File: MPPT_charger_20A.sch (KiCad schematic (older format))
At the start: 6 parts, among them J5 CONN_01X03

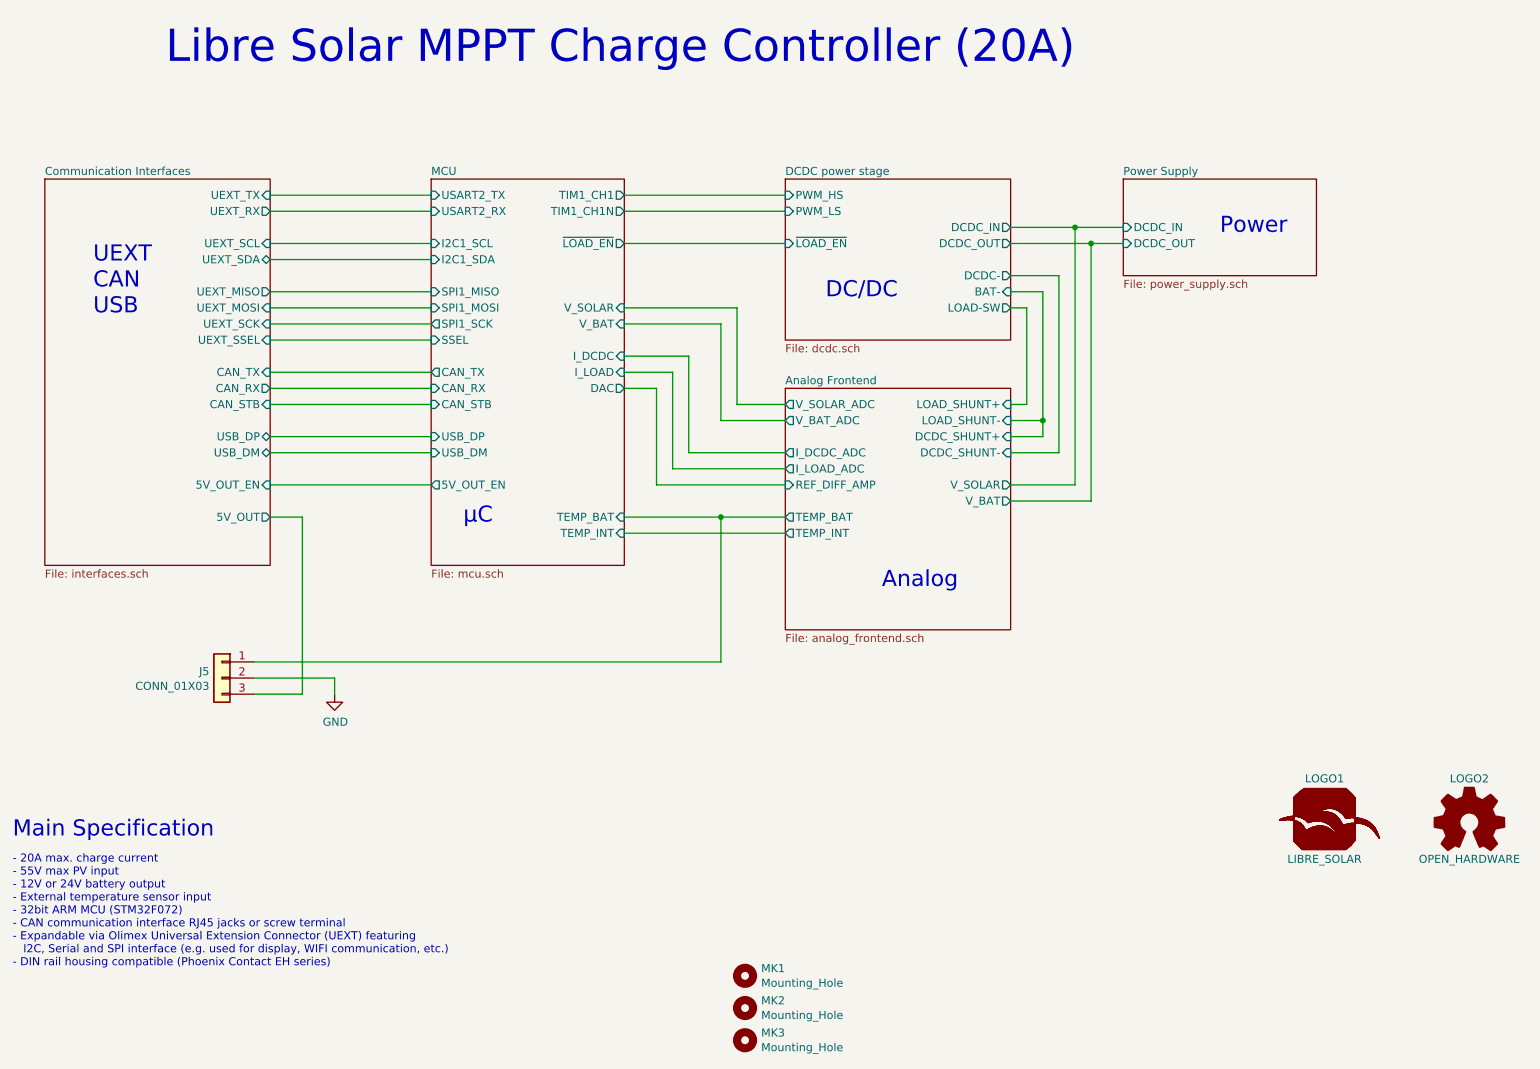
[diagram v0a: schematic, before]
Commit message: Bus power supply from battery instead of 10V rail
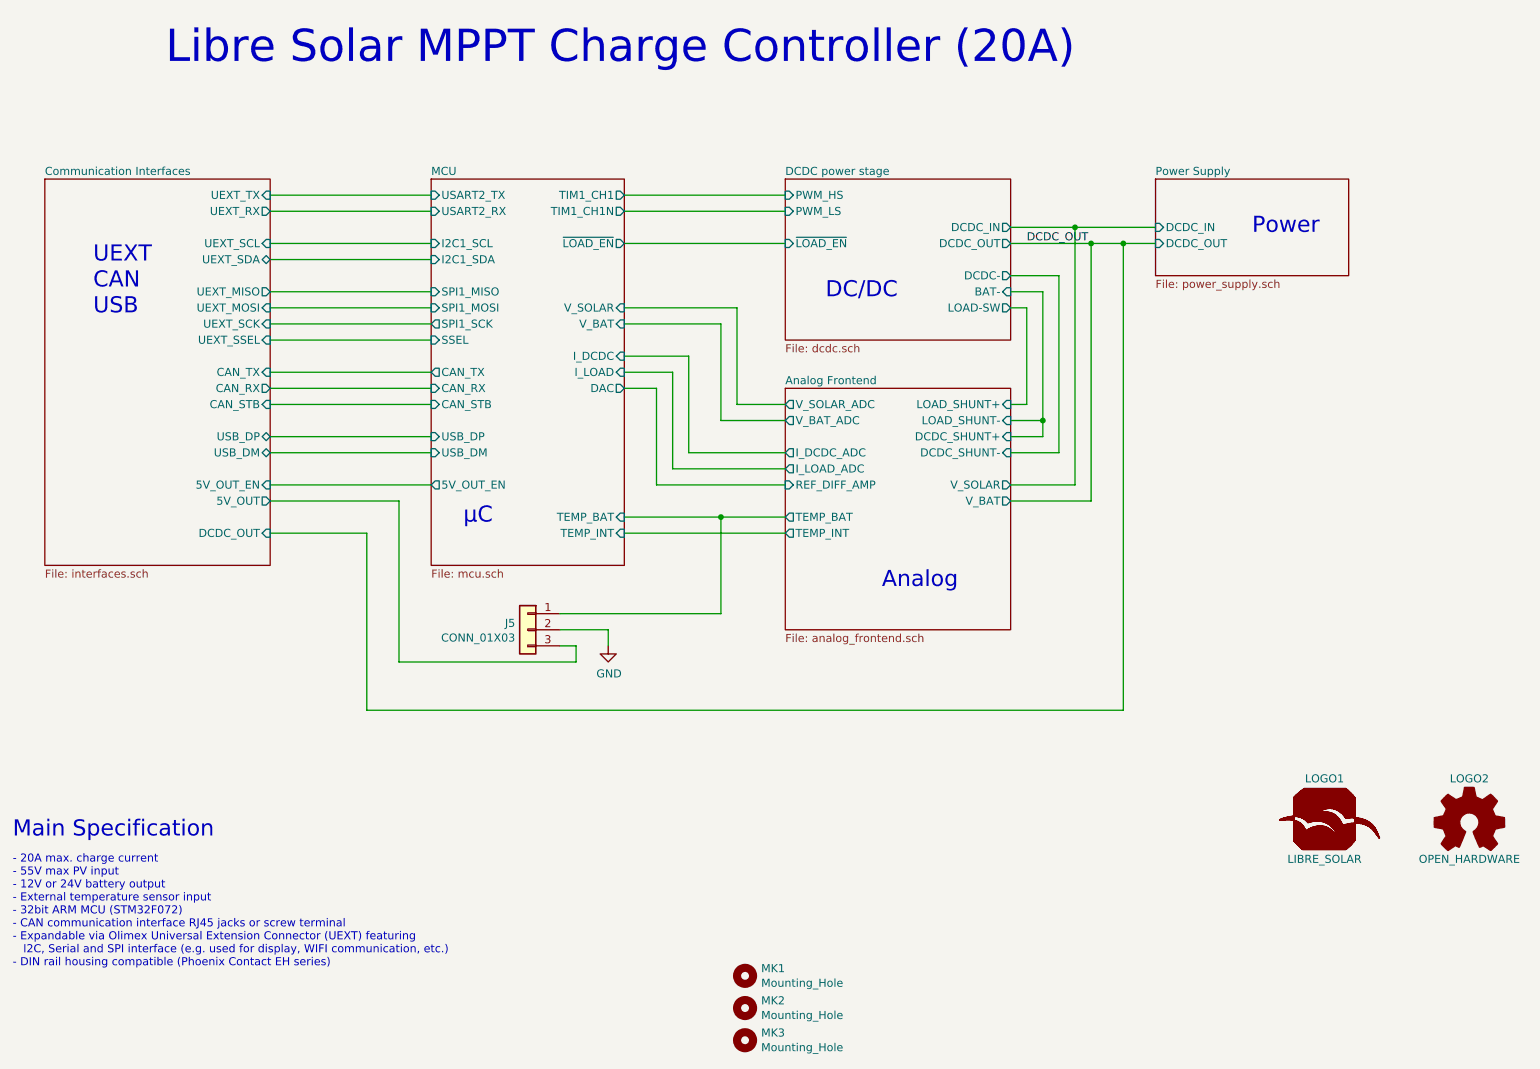
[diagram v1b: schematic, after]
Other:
- moved on the sheet: J5
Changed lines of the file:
@@
 $EndSheet
 $Sheet
-S 8400 2100 1200 600
+S 8600 2100 1200 600
 U 58C18D5C
 F0 "Power Supply" 50
 F1 "power_supply.sch" 50
-F2 "DCDC_OUT" I L 8400 2500 50
-F3 "DCDC_IN" I L 8400 2400 50
+F2 "DCDC_OUT" I L 8600 2500 50
+F3 "DCDC_IN" I L 8600 2400 50
 $EndSheet
 Wire Wire Line
@@
 F13 "CAN_TX" I R 3100 3300 50
 F14 "CAN_STB" I R 3100 3500 50
-F15 "5V_OUT" O R 3100 4200 50
+F15 "5V_OUT" O R 3100 4100 50
 F16 "5V_OUT_EN" I R 3100 4000 50
+F17 "DCDC_OUT" I R 3100 4300 50
 $EndSheet
 Wire Wire Line
@@
 $EndComp
 Wire Wire Line
-	7700 2400 8400 2400
-Wire Wire Line
-	7700 2500 8400 2500
+	7700 2400 8600 2400
+Wire Wire Line
+	7700 2500 8600 2500
 $Sheet
 S 6300 3400 1400 1500
@@
 Text Notes 6900 4650 0    100  ~ 0
 Analog
-Text Notes 9000 2450 0    100  ~ 0
+Text Notes 9200 2450 0    100  ~ 0
 Power
 Wire Wire Line
@@
 	5500 4000 6300 4000
 Wire Wire Line
-	6300 4200 5300 4200
+	5300 4200 6300 4200
 Wire Wire Line
 	5300 4300 6300 4300
@@
 L Connector:Conn_01x03 J5
 U 1 1 59553D8B
-P 2800 5200
-F 0 "J5" H 2878 5241 50  0000 L CNN
-F 1 "CONN_01X03" H 2878 5150 50  0000 L CNN
-F 2 "LibreSolar:Phoenix_Contact_MC_1,5_3-G-3,81" H 2800 5200 50  0001 C CNN
-F 3 "" H 2800 5200 50  0001 C CNN
-F 4 "Phoenix Contact" H 0   0   60  0001 C CNN "Manufacturer"
-F 5 "1803280" H 0   0   60  0001 C CNN "PartNumber"
-	1    2800 5200
+P 4700 4900
+F 0 "J5" H 4778 4941 50  0000 L CNN
+F 1 "CONN_01X03" H 4778 4850 50  0000 L CNN
+F 2 "LibreSolar:Phoenix_Contact_MC_1,5_3-G-3,81" H 4700 4900 50  0001 C CNN
+F 3 "" H 4700 4900 50  0001 C CNN
+F 4 "Phoenix Contact" H 1900 -300 60  0001 C CNN "Manufacturer"
+F 5 "1803280" H 1900 -300 60  0001 C CNN "PartNumber"
+	1    4700 4900
 	-1   0    0    -1
 $EndComp
@@
 L power:GND #PWR01
 U 1 1 59553D94
-P 3500 5300
-F 0 "#PWR01" H 3500 5050 50  0001 C CNN
-F 1 "GND" H 3505 5127 50  0000 C CNN
-F 2 "" H 3500 5300 50  0001 C CNN
-F 3 "" H 3500 5300 50  0001 C CNN
-	1    3500 5300
-	1    0    0    -1
-$EndComp
-Wire Wire Line
-	3000 5100 5900 5100
-Wire Wire Line
-	5900 5100 5900 4200
+P 5200 5000
+F 0 "#PWR01" H 5200 4750 50  0001 C CNN
+F 1 "GND" H 5205 4827 50  0000 C CNN
+F 2 "" H 5200 5000 50  0001 C CNN
+F 3 "" H 5200 5000 50  0001 C CNN
+	1    5200 5000
+	1    0    0    -1
+$EndComp
+Wire Wire Line
+	4900 4800 5900 4800
+Wire Wire Line
+	5900 4800 5900 4200
 Connection ~ 5900 4200
 Wire Wire Line
-	3000 5200 3500 5200
-Wire Wire Line
-	3500 5200 3500 5300
-Wire Wire Line
-	3100 4200 3300 4200
-Wire Wire Line
-	3300 4200 3300 5300
-Wire Wire Line
-	3300 5300 3000 5300
+	4900 4900 5200 4900
+Wire Wire Line
+	5200 4900 5200 5000
+Wire Wire Line
+	5000 5000 4900 5000
 Wire Wire Line
 	3100 4000 4100 4000
+Wire Wire Line
+	5000 5000 5000 5100
+Wire Wire Line
+	5000 5100 3900 5100
+Wire Wire Line
+	3900 5100 3900 4100
+Wire Wire Line
+	3900 4100 3100 4100
+Wire Wire Line
+	3100 4300 3700 4300
+Wire Wire Line
+	3700 4300 3700 5400
+Wire Wire Line
+	3700 5400 8400 5400
+Wire Wire Line
+	8400 5400 8400 2500
+Connection ~ 8400 2500
+Text Label 7800 2500 0    50   ~ 0
+DCDC_OUT
 $EndSCHEMATC

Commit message: Revision 0.9 for first small production batch - Switchable power supply for bus and UEXT (to be make sure to reach very low power consumption during LVD conditions) - MLCCs for EMC added to each high power input/output - Re-arrangement of some connectors after initial tests with housing
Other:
- note added: "- 12V or 24V battery voltage\n- 20A max. charge current\n- 55V max. solar input\n- External temperature sensor input\n- 32bit ARM MCU (STM32F072)\n- CAN communication interface RJ45 jacks incl. bus power supply\n- Expandable via Olimex Universal Extension Connector (UEXT) featuring\n I2C, Serial and SPI interface (e.g. used for display, WIFI communication, etc.)\n- Prepared for Hammond Mfg. 1591X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"
- note added: "MCU"
- note added: "UEXT\n\nCAN\n\nUSB"
- note removed: "- 20A max. charge current\n- 55V max PV input\n- 12V or 24V battery output\n- External temperature sensor input\n- 32bit ARM MCU (STM32F072)\n- CAN communication interface RJ45 jacks or screw terminal\n- Expandable via Olimex Universal Extension Connector (UEXT) featuring\n I2C, Serial and SPI interface (e.g. used for display, WIFI communication, etc.)\n- DIN rail housing compatible (Phoenix Cont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"
- note removed: "UEXT\nCAN\nUSB"
- note removed: "µC"
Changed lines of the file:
@@
 Sheet 1 6
 Title "MPPT Charger 20A"
-Date "2017-03-06"
-Rev "0.7"
+Date "2017-12-11"
+Rev "0.9"
 Comp "Libre Solar"
 Comment1 "Author: Martin Jäger"
@@
 F2 "PWM_HS" I L 6300 2200 50
 F3 "PWM_LS" I L 6300 2300 50
-F4 "~LOAD_EN" I L 6300 2500 50
-F5 "BAT-" I R 7700 2800 50
-F6 "DCDC_OUT" O R 7700 2500 50
-F7 "DCDC_IN" O R 7700 2400 50
-F8 "LOAD-SW" O R 7700 2900 50
-F9 "DCDC-" O R 7700 2700 50
+F4 "BAT-" I R 7700 2800 50
+F5 "DCDC_OUT" O R 7700 2500 50
+F6 "DCDC_IN" O R 7700 2400 50
+F7 "DCDC-" O R 7700 2700 50
+F8 "~LOAD_EN" I L 6300 2500 50
+F9 "LOAD-SW" O R 7700 2900 50
 $EndSheet
 $Sheet
@@
 F4 "V_BAT" I R 5300 3000 50
 F5 "V_SOLAR" I R 5300 2900 50
-F6 "~LOAD_EN" O R 5300 2500 50
-F7 "I_LOAD" I R 5300 3300 50
-F8 "I_DCDC" I R 5300 3200 50
-F9 "CAN_TX" O L 4100 3300 50
-F10 "CAN_RX" I L 4100 3400 50
-F11 "I2C1_SDA" I L 4100 2600 50
-F12 "I2C1_SCL" I L 4100 2500 50
-F13 "SPI1_MOSI" I L 4100 2900 50
-F14 "SPI1_MISO" I L 4100 2800 50
-F15 "SPI1_SCK" O L 4100 3000 50
-F16 "SSEL" I L 4100 3100 50
-F17 "USB_DM" I L 4100 3800 50
-F18 "USB_DP" I L 4100 3700 50
-F19 "CAN_STB" I L 4100 3500 50
-F20 "USART2_RX" I L 4100 2300 50
-F21 "USART2_TX" I L 4100 2200 50
-F22 "TEMP_INT" I R 5300 4300 50
-F23 "TEMP_BAT" I R 5300 4200 50
-F24 "DAC" O R 5300 3400 50
-F25 "5V_OUT_EN" O L 4100 4000 50
+F6 "I_LOAD" I R 5300 3300 50
+F7 "I_DCDC" I R 5300 3200 50
+F8 "CAN_TX" O L 4100 3300 50
+F9 "CAN_RX" I L 4100 3400 50
+F10 "I2C1_SDA" I L 4100 2600 50
+F11 "I2C1_SCL" I L 4100 2500 50
+F12 "SPI1_MOSI" I L 4100 2900 50
+F13 "SPI1_MISO" I L 4100 2800 50
+F14 "SPI1_SCK" O L 4100 3000 50
+F15 "SSEL" I L 4100 3100 50
+F16 "USB_DM" I L 4100 3800 50
+F17 "USB_DP" I L 4100 3700 50
+F18 "CAN_STB" I L 4100 3500 50
+F19 "USART2_RX" I L 4100 2300 50
+F20 "USART2_TX" I L 4100 2200 50
+F21 "TEMP_INT" I R 5300 4300 50
+F22 "TEMP_BAT" I R 5300 4200 50
+F23 "DAC" O R 5300 3400 50
+F24 "5V_OUT_EN" O L 4100 4200 50
+F25 "UEXT_EN" O L 4100 4000 50
+F26 "V_BUS_EN" O L 4100 4100 50
+F27 "~LOAD_EN" O R 5300 2500 50
 $EndSheet
 $Sheet
@@
 F0 "Power Supply" 50
 F1 "power_supply.sch" 50
-F2 "DCDC_OUT" I L 8600 2500 50
-F3 "DCDC_IN" I L 8600 2400 50
+F2 "DCDC_IN" I L 8600 2400 50
 $EndSheet
 Wire Wire Line
@@
 	6300 2300 5300 2300
 $Sheet
-S 1700 2100 1400 2400
+S 1700 2100 1400 2600
 U 58BE3089
 F0 "Communication Interfaces" 50
@@
 F13 "CAN_TX" I R 3100 3300 50
 F14 "CAN_STB" I R 3100 3500 50
-F15 "5V_OUT" O R 3100 4100 50
-F16 "5V_OUT_EN" I R 3100 4000 50
-F17 "DCDC_OUT" I R 3100 4300 50
+F15 "5V_OUT" O R 3100 4300 50
+F16 "5V_OUT_EN" I R 3100 4200 50
+F17 "DCDC_OUT" I R 3100 4500 50
+F18 "UEXT_EN" I R 3100 4000 50
+F19 "V_BUS_EN" I R 3100 4100 50
 $EndSheet
 Wire Wire Line
@@
 Main Specification
 Text Notes 1500 7000 0    50   ~ 0
-- 20A max. charge current\n- 55V max PV input\n- 12V or 24V battery output\n- External temperature sensor input\n- 32bit ARM MCU (STM32F072)\n- CAN communication interface RJ45 jacks or screw terminal\n- Expandable via Olimex Universal Extension Connector (UEXT) featuring\n   I2C, Serial and SPI interface (e.g. used for display, WIFI communication, etc.)\n- DIN rail housing compatible (Phoenix Contact EH series)\n
+- 12V or 24V battery voltage\n- 20A max. charge current\n- 55V max. solar input\n- External temperature sensor input\n- 32bit ARM MCU (STM32F072)\n- CAN communication interface RJ45 jacks incl. bus power supply\n- Expandable via Olimex Universal Extension Connector (UEXT) featuring\n   I2C, Serial and SPI interface (e.g. used for display, WIFI communication, etc.)\n- Prepared for Hammond Mfg. 1591XXCFL enclosure\n
 $Comp
 L Graphic:Logo_Open_Hardware_Small LOGO2
@@
 Wire Wire Line
 	7700 2400 8600 2400
-Wire Wire Line
-	7700 2500 8600 2500
 $Sheet
 S 6300 3400 1400 1500
@@
 F14 "REF_DIFF_AMP" I L 6300 4000 50
 $EndSheet
-Text Notes 2000 2950 0    100  ~ 0
-UEXT\nCAN\nUSB
+Text Notes 2000 3400 0    100  ~ 0
+UEXT\n\nCAN\n\nUSB
 Wire Wire Line
 	5300 2500 6300 2500
 Text Notes 6550 2850 0    100  ~ 0
 DC/DC
-Text Notes 4300 4250 0    100  ~ 0
-µC
+Text Notes 4800 3750 0    100  ~ 0
+MCU
 Text Notes 6900 4650 0    100  ~ 0
 Analog
@@
 Connection ~ 8100 2400
 Wire Wire Line
-	8200 2500 8200 4100
+	8200 2500 8200 5400
 Wire Wire Line
 	8200 4100 7700 4100
-Connection ~ 8200 2500
 $Comp
 L Mechanical:Mounting_Hole MK1
@@
 	5000 5000 4900 5000
 Wire Wire Line
+	3100 4200 4100 4200
+Wire Wire Line
+	5000 5000 5000 5100
+Wire Wire Line
+	5000 5100 3900 5100
+Wire Wire Line
+	3900 5100 3900 4300
+Wire Wire Line
+	3900 4300 3100 4300
+Wire Wire Line
+	3100 4500 3700 4500
+Wire Wire Line
+	3700 4500 3700 5400
+Wire Wire Line
+	3700 5400 8200 5400
+Text Label 8200 5000 1    50   ~ 0
+DCDC_OUT
+Wire Wire Line
 	3100 4000 4100 4000
 Wire Wire Line
-	5000 5000 5000 5100
-Wire Wire Line
-	5000 5100 3900 5100
-Wire Wire Line
-	3900 5100 3900 4100
-Wire Wire Line
-	3900 4100 3100 4100
-Wire Wire Line
-	3100 4300 3700 4300
-Wire Wire Line
-	3700 4300 3700 5400
-Wire Wire Line
-	3700 5400 8400 5400
-Wire Wire Line
-	8400 5400 8400 2500
-Connection ~ 8400 2500
-Text Label 7800 2500 0    50   ~ 0
-DCDC_OUT
+	4100 4100 3100 4100
+Wire Wire Line
+	8200 2500 7700 2500
+Connection ~ 8200 4100
 $EndSCHEMATC

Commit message: Final version for Jan/2018 production
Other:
- note added: "Main Specifications"
- note removed: "Main Specification"
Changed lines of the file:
@@
 Sheet 1 6
 Title "MPPT Charger 20A"
-Date "2017-12-11"
-Rev "0.9"
+Date "2018-01-18"
+Rev "0.10"
 Comp "Libre Solar"
 Comment1 "Author: Martin Jäger"
@@
 Text Notes 2450 1400 0    200  ~ 0
 Libre Solar MPPT Charge Controller (20A)
-Text Notes 1500 6200 0    100  ~ 0
-Main Specification
+Text Notes 1500 6100 0    100  ~ 0
+Main Specifications
 Text Notes 1500 7000 0    50   ~ 0
-- 12V or 24V battery voltage\n- 20A max. charge current\n- 55V max. solar input\n- External temperature sensor input\n- 32bit ARM MCU (STM32F072)\n- CAN communication interface RJ45 jacks incl. bus power supply\n- Expandable via Olimex Universal Extension Connector (UEXT) featuring\n   I2C, Serial and SPI interface (e.g. used for display, WIFI communication, etc.)\n- Prepared for Hammond Mfg. 1591XXCFL enclosure\n
+- 12V or 24V battery voltage\n- 20A max. charge current\n- 55V max. solar input\n- External temperature sensor input\n- 32bit ARM MCU (STM32F072)\n- CAN communication interface RJ45 jacks incl. bus power supply\n- Expandable via Olimex Universal Extension Connector (UEXT) featuring\n   I2C, Serial and SPI interface (e.g. used for display, WIFI communication, etc.)\n- Prepared for Hammond Mfg. 1591XXCFL enclosure\n   (light pipe of 30.5 mm length should be used for SMD LEDs, e.g. Bivar PLP2-1200)\n
 $Comp
 L Graphic:Logo_Open_Hardware_Small LOGO2

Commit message: Update to KiCad 5 schematic library
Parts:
- J5: symbol Connector:Conn_01x03 -> Connector_Generic:Conn_01x03
- LOGO1: symbol LibreSolar:LIBRE_SOLAR -> Project:LibreSolar_Logo
- LOGO2: footprint Symbols:OSHW-Logo_5.7x6mm_SilkScreen -> Symbol:OSHW-Logo_5.7x6mm_SilkScreen
- MK1, MK2, MK3: footprint Mounting_Holes:MountingHole_3.2mm_M3 -> MountingHole:MountingHole_3.2mm_M3
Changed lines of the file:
@@
 F 0 "LOGO2" H 10550 6375 50  0000 C CNN
 F 1 "OPEN_HARDWARE" H 10550 5875 50  0000 C CNN
-F 2 "Symbols:OSHW-Logo_5.7x6mm_SilkScreen" H 10550 6100 60  0001 C CNN
+F 2 "Symbol:OSHW-Logo_5.7x6mm_SilkScreen" H 10550 6100 60  0001 C CNN
 F 3 "" H 10550 6100 60  0001 C CNN
 	1    10550 6100
@@
 $EndComp
 $Comp
-L LibreSolar:LIBRE_SOLAR LOGO1
+L Project:LibreSolar_Logo LOGO1
 U 1 1 58C39FC7
 P 9650 6100
@@
 $EndComp
 Wire Wire Line
-	7700 2400 8600 2400
+	7700 2400 8100 2400
 $Sheet
 S 6300 3400 1400 1500
@@
 	5500 4000 6300 4000
 Wire Wire Line
-	5300 4200 6300 4200
+	5300 4200 5900 4200
 Wire Wire Line
 	5300 4300 6300 4300
@@
 	7700 3600 7900 3600
 Wire Wire Line
-	7900 2800 7900 3700
+	7900 2800 7900 3600
 Wire Wire Line
 	7900 3700 7700 3700
@@
 Connection ~ 8100 2400
 Wire Wire Line
-	8200 2500 8200 5400
+	8200 2500 8200 4100
 Wire Wire Line
 	8200 4100 7700 4100
@@
 F 0 "MK1" H 6150 7096 50  0000 L CNN
 F 1 "Mounting_Hole" H 6150 7005 50  0000 L CNN
-F 2 "Mounting_Holes:MountingHole_3.2mm_M3" H 6050 7050 50  0001 C CNN
+F 2 "MountingHole:MountingHole_3.2mm_M3" H 6050 7050 50  0001 C CNN
 F 3 "" H 6050 7050 50  0001 C CNN
 	1    6050 7050
@@
 F 0 "MK2" H 6150 7296 50  0000 L CNN
 F 1 "Mounting_Hole" H 6150 7205 50  0000 L CNN
-F 2 "Mounting_Holes:MountingHole_3.2mm_M3" H 6050 7250 50  0001 C CNN
+F 2 "MountingHole:MountingHole_3.2mm_M3" H 6050 7250 50  0001 C CNN
 F 3 "" H 6050 7250 50  0001 C CNN
 	1    6050 7250
@@
 F 0 "MK3" H 6150 7496 50  0000 L CNN
 F 1 "Mounting_Hole" H 6150 7405 50  0000 L CNN
-F 2 "Mounting_Holes:MountingHole_3.2mm_M3" H 6050 7450 50  0001 C CNN
+F 2 "MountingHole:MountingHole_3.2mm_M3" H 6050 7450 50  0001 C CNN
 F 3 "" H 6050 7450 50  0001 C CNN
 	1    6050 7450
@@
 $EndComp
 $Comp
-L Connector:Conn_01x03 J5
+L Connector_Generic:Conn_01x03 J5
 U 1 1 59553D8B
 P 4700 4900
@@
 	8200 2500 7700 2500
 Connection ~ 8200 4100
+Wire Wire Line
+	7900 3600 7900 3700
+Wire Wire Line
+	8100 2400 8600 2400
+Wire Wire Line
+	5900 4200 6300 4200
+Wire Wire Line
+	8200 4100 8200 5400
 $EndSCHEMATC

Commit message: Note regarding development of new version added
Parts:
- MK1, MK2, MK3: symbol Mechanical:Mounting_Hole -> Mechanical:MountingHole
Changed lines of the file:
@@
 	8200 4100 7700 4100
 $Comp
-L Mechanical:Mounting_Hole MK1
+L Mechanical:MountingHole MK1
 U 1 1 595388B0
 P 6050 7050
@@
 $EndComp
 $Comp
-L Mechanical:Mounting_Hole MK2
+L Mechanical:MountingHole MK2
 U 1 1 59538A86
 P 6050 7250
@@
 $EndComp
 $Comp
-L Mechanical:Mounting_Hole MK3
+L Mechanical:MountingHole MK3
 U 1 1 59538C18
 P 6050 7450
